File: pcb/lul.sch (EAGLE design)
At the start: 35 parts, among them IC1 STM32F072C8T6, U1 UG-2864HSWEG01

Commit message: working on pcb
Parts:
- removed S18: ENCODER-SWITCH, SparkFun-Switches:ENCODER-SWITCH
- removed SJ1, SJ2: (no value), microbuilder:SOLDERJUMPERREFLOW_NOPASTE
- added IC2: REG1117, clock:REG1117
- added JP1: (no value), pinhead:PINHD-1X5
- added R1: (no value), clock:RESISTOR0805-RES
- added R10, R11, R12, R13, R14, R15, R16, R21, R5, R6, R7, R8, R9: 330, clock:RESISTOR0805-RES
- added R22, R4: 10k, clock:RESISTOR0805-RES
- added S19, S20, S21, S22: TAC_SWITCHSMD, clock:TAC_SWITCHSMD
- added U$1: N-CHANNEL-MOSFET-BSS138, basicBoard:N-CHANNEL-MOSFET-BSS138
- added X1: USB-MICROB, clock:USB-MICROB
- C3, C4, C5, C6, C7, C8: device microbuilder:CAP_CERAMIC0805 -> clock:CAP0805
- R17, R18: device SparkFun-Resistors:10KOHM-0603-1/10W-1% -> clock:RESISTOR0805-RES
- R19, R20: value 10k -> 330; device SparkFun-Resistors:10KOHM-0603-1/10W-1% -> clock:RESISTOR0805-RES
- R2: value 10K -> 10k; device microbuilder:RESISTOR0805 -> clock:RESISTOR0805-RES
- R3: device microbuilder:RESISTOR0805 -> clock:RESISTOR0805-RES
- S16: value MOMENTARY-SWITCH-SPST-LED-PTH-CHERRY -> ENCODER-SWITCH; device SparkFun-Switches:MOMENTARY-SWITCH-SPST-LED-PTH-CHERRY -> SparkFun-Switches:ENCODER-SWITCH
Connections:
- removed net 3.3V: C6.P$2, C7.P$2, R17.2, R18.2, R19.2, R20.2, SJ2.1, U1.VBAT, U1.VDD
- removed net ENCODER_R0: R19.1, S18.B
- removed net ENCODER_R1: R20.1, S18.A
- removed net R_SW: S18.SW+
- new net +3V3: C6.2, C7.2, IC1AN_POWER.VDDA, IC1POWER.VDD_1, IC1POWER.VDD_2, IC1POWER.VDD_3, IC2.VOUT, R10.2, R11.2, R12.2, R13.2, R14.2, R15.2, R16.2, R17.2, R18.2, R19.2, R20.2, R21.2, R4.2, R5.2, R6.2, R7.2, R8.2, R9.2, S22.3, S22.4, SD1.VDD, U1.BS1, U1.VBAT, U1.VDD
- new net N$10: IC1PORTA_L.PA6, SD1.DAT0(DO)
- new net N$13: IC1PORTA_L.PA7, SD1.CMD(DI)
- new net N$14: IC1PORTA_L.PA4, SD1.!CARD
- new net N$15: R5.1, S1.A
- new net N$16: R8.1, S4.A
- new net N$17: R11.1, S7.A
- new net N$18: R14.1, S10.A
- new net N$19: R19.1, S13.A
- new net N$20: R6.1, S2.A
- new net N$21: R9.1, S5.A
- new net N$22: R12.1, S8.A
- new net N$23: R15.1, S11.A
- new net N$24: R20.1, S14.A
- new net N$25: R7.1, S3.A
- new net N$26: R10.1, S6.A
- new net N$27: R13.1, S9.A
- new net N$28: R16.1, S12.A
- new net N$29: R21.1, S15.A
- new net N$30: S1.C, S10.C, S11.C, S12.C, S13.C, S14.C, S15.C, S2.C, S3.C, S4.C, S5.C, S6.C, S7.C, S8.C, S9.C, U$1.D
- new net N$31: R22.2, U$1.G
- new net N$8: IC1PORTA_L.PA5, SD1.CLK(SCLK)
- new net N$9: IC1RESET.NRST, R4.1, S21.1, S21.2
- new net SD_CS: IC1PORTB_L.PB0, SD1.CD/DAT3(!CS!)
- new net USB_DN: IC1PORTA_H.PA11, X1.D-
- new net USB_DP: IC1PORTA_H.PA12, X1.D+
- net D1/MOSI/SDA1_3.3V: now also U1.D2/I2C_SDA; no longer SJ1.1
- net GND: now also C5.1, C6.1, C7.1, C8.1, IC1AN_POWER.VBAT, IC1AN_POWER.VSSA, IC1POWER.VSS_1, IC1POWER.VSS_2, IC1POWER.VSS_3, IC2.GND, R22.1, S1.1, S10.1, S11.1, S12.1, S13.1, S14.1, S15.1, S2.1, S21.3, S21.4, S3.1, S4.1, S5.1, S6.1, S7.1, S8.1, S9.1, SD1.S1, SD1.S2, SD1.S3, SD1.S4, SD1.VSS, U$1.S, X1.GND; no longer C5.P$1, C6.P$1, C7.P$1, C8.P$1, S1.2, S10.2, S11.2, S12.2, S13.2, S14.2, S15.2, S16.2, S18.C, S18.SW-, S2.2, S3.2, S4.2, S5.2, S6.2, S7.2, S8.2, S9.2
- net N$1: now also IC2.VIN, X1.VBUS; no longer R2.2, SJ2.2, U1.BS1
- net N$11: now also C5.2; no longer C5.P$2
- net N$12: now also C8.2; no longer C8.P$2
- net N$2: now also IC1RESET.BOOT0, R2.2, S22.1, S22.2; no longer SJ1.2, U1.D2/I2C_SDA
- net N$4: now also C3.2; no longer C3.P$2
- net N$5: now also C3.1; no longer C3.P$1
- net N$6: now also C4.2; no longer C4.P$2
- net N$7: now also C4.1; no longer C4.P$1
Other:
- note removed: "Bus default = SPI4"
- note removed: "Close SJ2 for I2C"
- note removed: "Close for"
- note removed: "I2C"
- moved on the sheet: IC1AN_POWER, IC1PORTA_H, IC1PORTA_L, IC1PORTB_H, IC1PORTB_L, IC1PORTF/OSC, IC1POWER, IC1RESET, R19, R20, S1, S10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

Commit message: routing lulboard
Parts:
- removed R17, R18: 10k, clock:RESISTOR0805-RES
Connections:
- removed net ENCODER_L0: R17.1, S17.B
- removed net ENCODER_L1: R18.1, S17.A
- removed net L_SW: S17.SW+
- new net E1A: IC1PORTB_L.PB2, S17.A
- new net E1B: IC1PORTB_H.PB10, S17.B
- new net E1_SW: IC1PORTB_L.PB1, S17.SW+
- new net E2A: IC1PORTA_L.PA0, S16.A
- new net E2B: IC1PORTA_L.PA1, S16.B
- new net E2_SW: IC1PORTA_L.PA3, S16.SW-
- new net SW10: IC1PORTB_L.PB7, S10.2
- new net SW11: IC1PORTC.PC13, S11.2
- new net SW12: IC1PORTC.PC14, S12.2
- new net SW13: IC1PORTC.PC15, S13.2
- new net SW14: IC1PORTF/OSC.PF0/OSC<=, S14.2
- new net SW15: IC1PORTF/OSC.PF1/OSC=>, S15.2
- new net SW4: S4.2
- new net SW5: IC1PORTA_H.PA15, S5.2
- new net SW6: IC1PORTB_L.PB3, S6.2
- new net SW7: IC1PORTB_L.PB4, S7.2
- new net SW8: IC1PORTB_L.PB5, S8.2
- new net SW9: IC1PORTB_L.PB6, S9.2
- net +3V3: no longer R17.2, R18.2, S22.4
- net GND: now also S16.C, S16.SW+; no longer S21.3
- net N$2: no longer S22.2
- net N$9: no longer S21.1
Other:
- moved on the sheet: IC1PORTA_H, IC1PORTA_L, IC1PORTB_H, IC1PORTB_L, S16

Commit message: SLMOST FINISHED
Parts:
- removed R1: (no value), clock:RESISTOR0805-RES
- added C1, C10, C2, C9: 0.1uF, clock:CAP0805
- added R17: (no value), clock:RESISTOR0805-RES
- added U$8: TEMT6000, ProtoSnap-v14a:TEMT6000
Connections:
- removed net CS_3.3V: U1./CS
- removed net D0/SCLK/SCK_3.3V: U1.D0/SPI_SCLK/I2C_SCK
- removed net D1/MOSI/SDA1_3.3V: U1.D1/SPI_SDIN/I2C_SDA, U1.D2/I2C_SDA
- removed net DC/SA0_3.3V: U1.DC/I2C_SA0
- removed net N$31: R22.2, U$1.G
- removed net N$9: IC1RESET.NRST, R4.1, S21.2
- removed net RST_3.3V: U1./RES
- new net BACK_LIGHT: IC1PORTA_H.PA10, R22.2, U$1.G
- new net BUTTON1: IC1PORTB_H.PB12, S19.1, S19.2
- new net BUTTON2: IC1PORTB_H.PB11, S20.1, S20.2
- new net LIGHT_SENSOR_OUTPUT: IC1PORTA_L.PA2, R17.2, U$8.E1
- new net N$32: IC1PORTA_H.PA14, JP1.1
- new net N$34: IC1PORTA_H.PA13, JP1.2
- new net RST: IC1RESET.NRST, R4.1, S21.2, U1./RES
- new net SCL: IC1PORTB_H.PB8, U1.D0/SPI_SCLK/I2C_SCK
- new net SDA: IC1PORTB_H.PB9, U1.D1/SPI_SDIN/I2C_SDA, U1.D2/I2C_SDA
- new net SW1: IC1PORTB_H.PB15, S1.2
- new net SW2: IC1PORTB_H.PB14, S2.2
- new net SW3: IC1PORTB_H.PB13, S3.2
- new net UART1_TX: IC1PORTA_H.PA9, JP1.3
- net +3V3: now also C1.2, C10.2, C2.2, C9.2, JP1.4, U$8.C1
- net GND: now also C1.1, C10.1, C2.1, C9.1, JP1.5, R17.1, S19.3, S19.4, S20.3, S20.4
- net SW4: now also IC1PORTA_H.PA8
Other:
- moved on the sheet: JP1, S19, S20

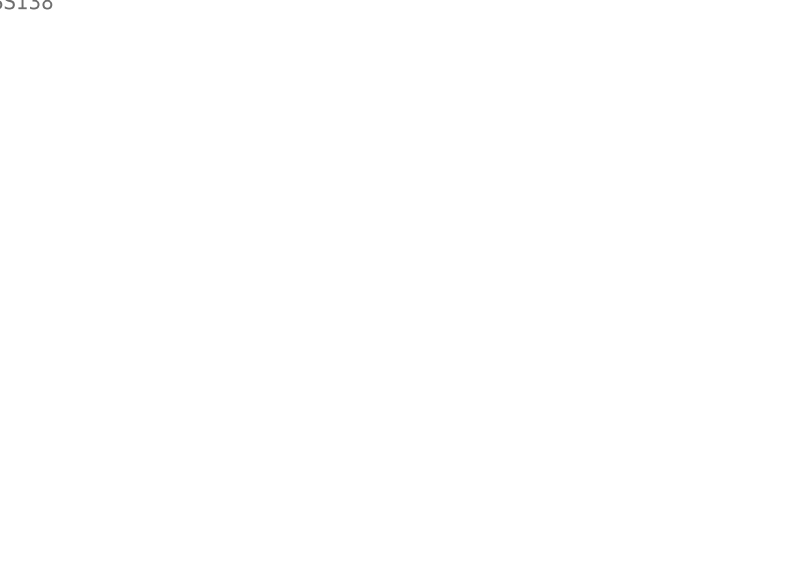
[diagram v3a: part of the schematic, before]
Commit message: w2812 working, before changing pcb to ws2812
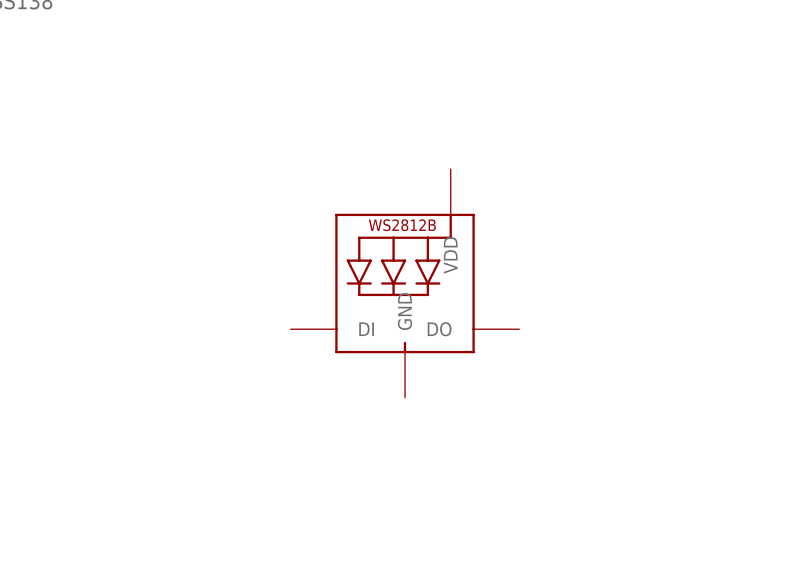
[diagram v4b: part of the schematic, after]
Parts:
- added LED1: WS2812B3535, adafruit:WS2812B3535
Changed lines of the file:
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@@
 <part name="GND45" library="backplane" deviceset="GND" device=""/>
 <part name="GND19" library="supply1" library_urn="urn:adsk.eagle:library:371" deviceset="GND" device=""/>
+<part name="LED1" library="adafruit" deviceset="WS2812B" device="3535"/>
 </parts>
 <sheets>
@@
 <instance part="GND45" gate="1" x="401.32" y="-76.2"/>
 <instance part="GND19" gate="1" x="154.94" y="-198.12"/>
+<instance part="LED1" gate="G$1" x="246.38" y="-127"/>
 </instances>
 <busses>

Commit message: before rotating
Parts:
- removed R10, R11, R12, R13, R14, R15, R16, R19, R20, R21, R5, R6, R7, R8, R9: 330, clock:RESISTOR0805-RES
- removed R22: 10k, clock:RESISTOR0805-RES
- removed U$1: N-CHANNEL-MOSFET-BSS138, basicBoard:N-CHANNEL-MOSFET-BSS138
- S1, S10, S11, S12, S13, S14, S15, S2, S3, S4, S5, S6, S7, S8, S9: device SparkFun-Switches:MOMENTARY-SWITCH-SPST-LED-PTH-CHERRY -> lul:MOMENTARY-SWITCH-SPST-LED-PTH-CHERRY
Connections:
- removed net N$15: R5.1, S1.A
- removed net N$16: R8.1, S4.A
- removed net N$17: R11.1, S7.A
- removed net N$18: R14.1, S10.A
- removed net N$19: R19.1, S13.A
- removed net N$20: R6.1, S2.A
- removed net N$21: R9.1, S5.A
- removed net N$22: R12.1, S8.A
- removed net N$23: R15.1, S11.A
- removed net N$24: R20.1, S14.A
- removed net N$25: R7.1, S3.A
- removed net N$26: R10.1, S6.A
- removed net N$27: R13.1, S9.A
- removed net N$28: R16.1, S12.A
- removed net N$29: R21.1, S15.A
- removed net N$30: S1.C, S10.C, S11.C, S12.C, S13.C, S14.C, S15.C, S2.C, S3.C, S4.C, S5.C, S6.C, S7.C, S8.C, S9.C, U$1.D
- net +3V3: no longer R10.2, R11.2, R12.2, R13.2, R14.2, R15.2, R16.2, R19.2, R20.2, R21.2, R5.2, R6.2, R7.2, R8.2, R9.2
- net BACK_LIGHT: no longer R22.2, U$1.G
- net GND: no longer R22.1, U$1.S

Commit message: routing finished
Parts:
- added C11, C12, C13, C14, C15, C16, C17, C18, C19, C20, C21, C22, C23, C24, C25, C26: 0.1uF, clock:CAP0805
- added C27: (no value), clock:C-USC1210
- added IC3: 74LVC1G125DBV, 74xx-little-de:74LVC1G125DBV
- added LED10, LED11, LED12, LED13, LED14, LED15, LED2, LED3, LED4, LED5, LED6, LED7, LED8, LED9: WS2812B3535, lul:WS2812B3535
- added R1, R5: 10k, clock:RESISTOR0805-RES
- added R6: 300, clock:RESISTOR0805-RES
- LED1: device adafruit:WS2812B3535 -> lul:WS2812B3535
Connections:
- removed net BACK_LIGHT: IC1PORTA_H.PA10
- removed net N$13: IC1PORTA_L.PA7, SD1.CMD(DI)
- new net LED_DATA_EN: IC1PORTA_H.PA10, IC3A.OE, R5.1
- new net N$15: LED1.DI, LED2.DO
- new net N$16: IC1PORTA_L.PA7, R6.1
- new net N$17: LED1.DO, LED4.DI
- new net N$18: LED4.DO, LED5.DI
- new net N$19: LED5.DO, LED6.DI
- new net N$20: LED6.DO, LED9.DI
- new net N$21: LED8.DI, LED9.DO
- new net N$22: LED7.DI, LED8.DO
- new net N$23: LED10.DI, LED7.DO
- new net N$24: LED10.DO, LED11.DI
- new net N$25: LED11.DO, LED12.DI
- new net N$26: LED12.DO, LED15.DI
- new net N$27: LED14.DI, LED15.DO
- new net N$28: LED13.DI, LED14.DO
- new net N$29: IC3A.O, LED3.DI, R1.2
- new net N$9: LED2.DI, LED3.DO
- new net SPI_MOSI: IC3A.I, R6.2, SD1.CMD(DI)
- net +3V3: now also C11.2, C12.2, C13.2, C14.2, C15.2, C16.2, C17.2, C18.2, C19.2, C20.2, C21.2, C22.2, C23.2, C24.2, C25.2, C26.2, C27.1, IC3P.VCC, LED1.VDD, LED10.VDD, LED11.VDD, LED12.VDD, LED13.VDD, LED14.VDD, LED15.VDD, LED2.VDD, LED3.VDD, LED4.VDD, LED5.VDD, LED6.VDD, LED7.VDD, LED8.VDD, LED9.VDD, R5.2
- net GND: now also C11.1, C12.1, C13.1, C14.1, C15.1, C16.1, C17.1, C18.1, C19.1, C20.1, C21.1, C22.1, C23.1, C24.1, C25.1, C26.1, C27.2, IC3P.GND, LED1.GND, LED10.GND, LED11.GND, LED12.GND, LED13.GND, LED14.GND, LED15.GND, LED2.GND, LED3.GND, LED4.GND, LED5.GND, LED6.GND, LED7.GND, LED8.GND, LED9.GND, R1.1, S1.2, S10.2, S11.2, S12.2, S13.2, S14.2, S15.2, S2.2, S3.2, S4.2, S5.2, S6.2, S7.2, S8.2, S9.2; no longer S1.1, S10.1, S11.1, S12.1, S13.1, S14.1, S15.1, S2.1, S3.1, S4.1, S5.1, S6.1, S7.1, S8.1, S9.1
- net SW1: now also IC1PORTB_H.PB13, S1.1; no longer IC1PORTB_H.PB15, S1.2
- net SW10: now also S10.1; no longer S10.2
- net SW11: now also S11.1; no longer S11.2
- net SW12: now also S12.1; no longer S12.2
- net SW13: now also S13.1; no longer S13.2
- net SW14: now also S14.1; no longer S14.2
- net SW15: now also S15.1; no longer S15.2
- net SW2: now also S2.1; no longer S2.2
- net SW3: now also IC1PORTB_H.PB15, S3.1; no longer IC1PORTB_H.PB13, S3.2
- net SW4: now also S4.1; no longer S4.2
- net SW5: now also S5.1; no longer S5.2
- net SW6: now also S6.1; no longer S6.2
- net SW7: now also S7.1; no longer S7.2
- net SW8: now also S8.1; no longer S8.2
- net SW9: now also S9.1; no longer S9.2
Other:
- moved on the sheet: S1, S10, S11, S12, S13, S14, S15, S2, S3, S4, S5, S6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

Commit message: seemingly finished
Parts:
- removed C26: 0.1uF, clock:CAP0805
- U1: device microbuilder:DISP_OLED_UG-2864HSWEG010.96" -> lul:DISP_OLED_UG-2864HSWEG010.96"
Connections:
- net +3V3: no longer C26.2
- net GND: no longer C26.1
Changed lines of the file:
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@@
 <part name="S14" library="lul" deviceset="MOMENTARY-SWITCH-SPST-LED" device="-PTH-CHERRY" value="MOMENTARY-SWITCH-SPST-LED-PTH-CHERRY"/>
 <part name="S15" library="lul" deviceset="MOMENTARY-SWITCH-SPST-LED" device="-PTH-CHERRY" value="MOMENTARY-SWITCH-SPST-LED-PTH-CHERRY"/>
-<part name="U1" library="microbuilder" deviceset="DISP_OLED_UG-2864HSWEG01" device="0.96&quot;" value="UG-2864HSWEG01"/>
+<part name="U1" library="lul" deviceset="DISP_OLED_UG-2864HSWEG01" device="0.96&quot;" value="UG-2864HSWEG01"/>
 <part name="U$2" library="supply1" library_urn="urn:adsk.eagle:library:371" deviceset="GND" device=""/>
 <part name="R3" library="clock" deviceset="RESISTOR" device="0805-RES" value="390K"/>
@@
 <part name="C24" library="clock" deviceset="CAP" device="0805" value="0.1uF"/>
 <part name="C25" library="clock" deviceset="CAP" device="0805" value="0.1uF"/>
-<part name="C26" library="clock" deviceset="CAP" device="0805" value="0.1uF"/>
 <part name="U$6" library="supply1" library_urn="urn:adsk.eagle:library:371" deviceset="GND" device=""/>
 <part name="+3V30" library="supply1" library_urn="urn:adsk.eagle:library:371" deviceset="+3V3" device=""/>
@@
 <instance part="C24" gate="G$1" x="-269.24" y="-35.56" rot="R180"/>
 <instance part="C25" gate="G$1" x="-259.08" y="-35.56" rot="R180"/>
-<instance part="C26" gate="G$1" x="-246.38" y="-35.56" rot="R180"/>
 <instance part="U$6" gate="1" x="-264.16" y="-43.18"/>
 <instance part="+3V30" gate="G$1" x="-264.16" y="-30.48"/>
@@
 </segment>
 <segment>
-<pinref part="C26" gate="G$1" pin="1"/>
 <pinref part="C25" gate="G$1" pin="1"/>
 <wire x1="-246.38" y1="-40.64" x2="-238.76" y2="-40.64" width="0.1524" layer="91"/>
@@
 <wire x1="-269.24" y1="-33.02" x2="-264.16" y2="-33.02" width="0.1524" layer="91"/>
 <junction x="-269.24" y="-33.02"/>
-<pinref part="C26" gate="G$1" pin="2"/>
 <wire x1="-264.16" y1="-33.02" x2="-259.08" y2="-33.02" width="0.1524" layer="91"/>
 <wire x1="-259.08" y1="-33.02" x2="-238.76" y2="-33.02" width="0.1524" layer="91"/>

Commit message: adjusted for both 0.96 and 1.3 inch oled
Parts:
- added TP1, TP2: TEST-POINT3X5, clock:TEST-POINT3X5
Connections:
- net GND: now also U1.D3, U1.D4, U1.D5, U1.D6, U1.D7, U1.E/RD, U1.R/W
- net N$29: now also TP1.1
- net SPI_MOSI: now also TP2.1
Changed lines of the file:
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@@
 <part name="+3V32" library="supply1" library_urn="urn:adsk.eagle:library:371" deviceset="+3V3" device=""/>
 <part name="C27" library="clock" deviceset="C-US" device="C1210"/>
+<part name="TP1" library="clock" deviceset="TEST-POINT" device="3X5"/>
+<part name="TP2" library="clock" deviceset="TEST-POINT" device="3X5"/>
 </parts>
 <sheets>
@@
 <instance part="+3V32" gate="G$1" x="-50.8" y="50.8" rot="MR0"/>
 <instance part="C27" gate="G$1" x="-238.76" y="-35.56"/>
+<instance part="TP1" gate="G$1" x="-73.66" y="30.48" smashed="yes" rot="R90"/>
+<instance part="TP2" gate="G$1" x="-40.64" y="30.48" smashed="yes" rot="R90"/>
 </instances>
 <busses>
@@
 <pinref part="C8" gate="G$1" pin="1"/>
 <pinref part="U$21" gate="1" pin="GND"/>
+<pinref part="U1" gate="G$1" pin="D3"/>
+<wire x1="363.22" y1="20.32" x2="325.12" y2="20.32" width="0.1524" layer="91"/>
+<wire x1="325.12" y1="20.32" x2="325.12" y2="17.78" width="0.1524" layer="91"/>
+<junction x="325.12" y="7.62"/>
+<pinref part="U1" gate="G$1" pin="D4"/>
+<wire x1="325.12" y1="17.78" x2="325.12" y2="15.24" width="0.1524" layer="91"/>
+<wire x1="325.12" y1="15.24" x2="325.12" y2="12.7" width="0.1524" layer="91"/>
+<wire x1="325.12" y1="12.7" x2="325.12" y2="10.16" width="0.1524" layer="91"/>
+<wire x1="325.12" y1="10.16" x2="325.12" y2="7.62" width="0.1524" layer="91"/>
+<wire x1="363.22" y1="17.78" x2="325.12" y2="17.78" width="0.1524" layer="91"/>
+<junction x="325.12" y="17.78"/>
+<pinref part="U1" gate="G$1" pin="D5"/>
+<wire x1="363.22" y1="15.24" x2="325.12" y2="15.24" width="0.1524" layer="91"/>
+<junction x="325.12" y="15.24"/>
+<pinref part="U1" gate="G$1" pin="D6"/>
+<wire x1="363.22" y1="12.7" x2="325.12" y2="12.7" width="0.1524" layer="91"/>
+<junction x="325.12" y="12.7"/>
+<pinref part="U1" gate="G$1" pin="D7"/>
+<wire x1="363.22" y1="10.16" x2="325.12" y2="10.16" width="0.1524" layer="91"/>
+<junction x="325.12" y="10.16"/>
+<pinref part="U1" gate="G$1" pin="E/RD"/>
+<wire x1="363.22" y1="30.48" x2="325.12" y2="30.48" width="0.1524" layer="91"/>
+<wire x1="325.12" y1="30.48" x2="325.12" y2="20.32" width="0.1524" layer="91"/>
+<junction x="325.12" y="20.32"/>
+<pinref part="U1" gate="G$1" pin="R/W"/>
+<wire x1="363.22" y1="33.02" x2="325.12" y2="33.02" width="0.1524" layer="91"/>
+<wire x1="325.12" y1="33.02" x2="325.12" y2="30.48" width="0.1524" layer="91"/>
+<junction x="325.12" y="30.48"/>
 </segment>
 <segment>
@@
 <wire x1="-73.66" y1="22.86" x2="-68.58" y2="22.86" width="0.1524" layer="91"/>
 <junction x="-73.66" y="22.86"/>
+<pinref part="TP1" gate="G$1" pin="1"/>
+<wire x1="-73.66" y1="30.48" x2="-73.66" y2="22.86" width="0.1524" layer="91"/>
 </segment>
 </net>
@@
 <wire x1="-40.64" y1="22.86" x2="-55.88" y2="22.86" width="0.1524" layer="91"/>
 <label x="-53.34" y="22.86" size="1.778" layer="95"/>
-</segment>
-<segment>
+<pinref part="TP2" gate="G$1" pin="1"/>
+<wire x1="-40.64" y1="30.48" x2="-40.64" y2="22.86" width="0.1524" layer="91"/>
+</segment>
+<segment>
